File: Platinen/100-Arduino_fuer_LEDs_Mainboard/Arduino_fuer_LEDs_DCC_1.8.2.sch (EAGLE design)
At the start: 116 parts, among them CON5 M04B4B-ZR4P, IC1 7805, IC2 LM393N, IC3 74125N, IC4 MCP2515-I/P, IC5 ISO1050, IC6 B0505S-1W, J1 day /night, J2 LocoNet, J3 SOLDERJUMPERNO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

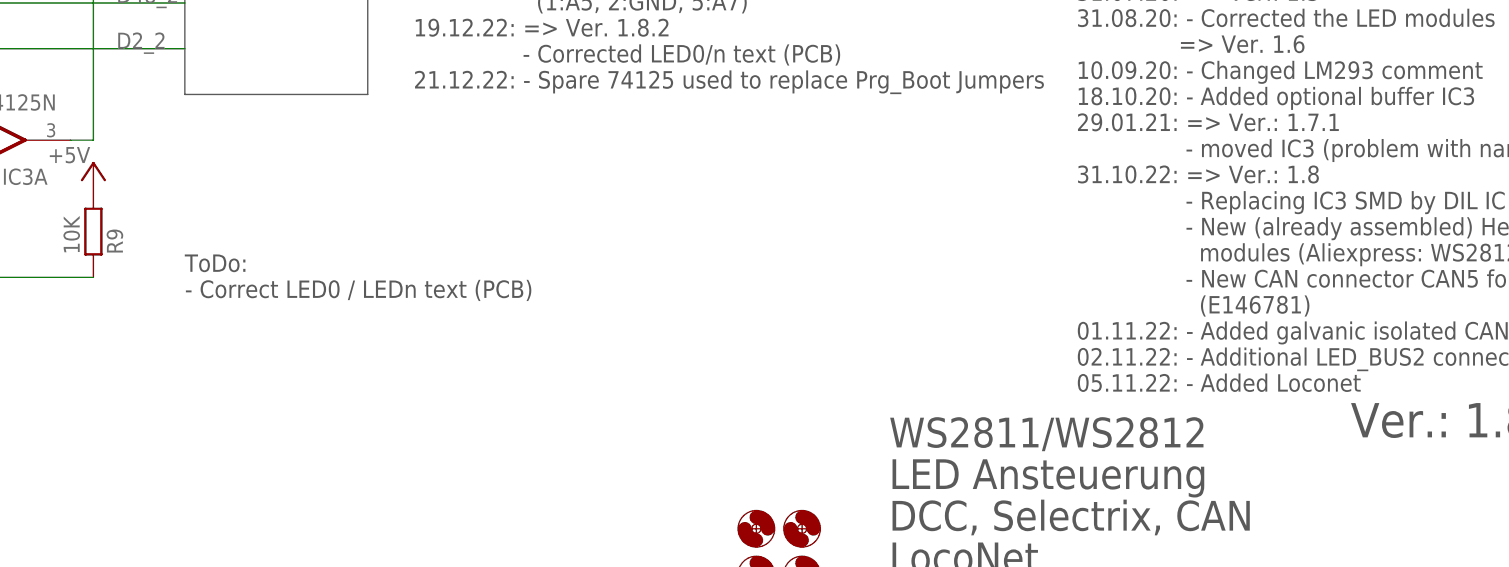
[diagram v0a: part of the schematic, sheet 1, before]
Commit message: Update Arduino_fuer_LEDs_DCC_1.8.2.sch
Updated Comments
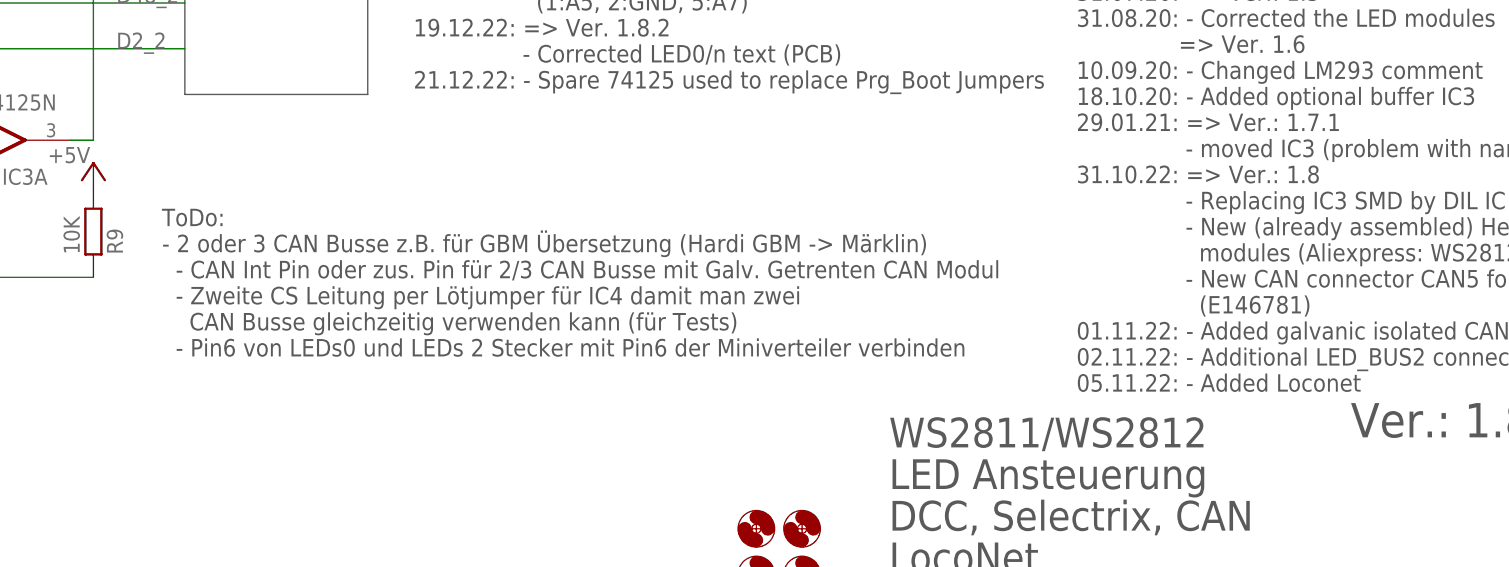
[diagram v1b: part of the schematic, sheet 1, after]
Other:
- note added: "ToDo: - 2 oder 3 CAN Busse z.B. für GBM Übersetzung (Hardi GBM -> Märklin) - CAN Int Pin oder zus. Pin für 2/3 CAN Busse mit Galv. Getrenten CAN Modul - Zweite CS Leitung per Lötjumper für IC4 damit man zwei CAN Busse gleichzeitig verwenden kann (für Tests) - Pin6 von LEDs0 und LEDs 2 Stecker mit Pin6 der Miniverteiler verbinden"
- note removed: "ToDo: - Correct LED0 / LEDn text (PCB)"
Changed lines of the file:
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@@
 <text x="78.232" y="219.71" size="1.524" layer="97">Pins für optionale
 Erweiterung ESP32</text>
-<text x="109.22" y="10.16" size="1.9304" layer="97" align="top-left">ToDo:
-- Correct LED0 / LEDn text (PCB)</text>
+<text x="106.68" y="15.24" size="1.9304" layer="97" align="top-left">ToDo:
+- 2 oder 3 CAN Busse z.B. für GBM Übersetzung (Hardi GBM -&gt; Märklin)
+  - CAN Int Pin oder zus. Pin für 2/3 CAN Busse mit Galv. Getrenten CAN Modul
+  - Zweite CS Leitung per Lötjumper für IC4 damit man zwei
+    CAN Busse gleichzeitig verwenden kann (für Tests)
+  - Pin6 von LEDs0 und LEDs 2 Stecker mit Pin6 der Miniverteiler verbinden</text>
 <text x="59.182" y="45.974" size="1.778" layer="97">LN TX</text>
 </plain>
